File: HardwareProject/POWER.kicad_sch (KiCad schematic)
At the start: 42 parts, among them U11 TPS54302, U12 LP5907MFX-3.3, U13 REF3030, U14 LM5164DDA, U15 SY8089

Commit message: 修改了UCC27211A封装，此芯片此前的封装均错误 修改了采样线布局，为SAR ADC加入前置RC
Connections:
- net +5V: now also U12.3 (EN)
- net at C62.1, FB5.2, U12.1 (IN): no longer U12.3 (EN)
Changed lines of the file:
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@@
-	)
-	(junction
-		(at 74.93 27.94)
-		(diameter 0)
-		(color 0 0 0 0)
 	)
 	(junction
@@
 		(pts
 			(xy 100.33 130.81) (xy 105.41 130.81)
-		)
-		(stroke
-			(width 0)
-			(type default)
-		)
-	)
-	(wire
-		(pts
-			(xy 74.93 27.94) (xy 74.93 30.48)
 		)
 		(stroke
@@
 					(unit 1)
 				)
+			)
+		)
+	)
+	(symbol
+		(lib_id "power:+5V")
+		(at 74.93 30.48 180)
+		(unit 1)
+		(exclude_from_sim no)
+		(in_bom yes)
+		(on_board yes)
+		(dnp no)
+		(fields_autoplaced yes)
+		(property "Reference" "#PWR0190"
+			(at 74.93 26.67 0)
+			(effects
+				(font
+					(size 1.27 1.27)
+				)
+				(hide yes)
+			)
+		)
+		(property "Value" "+5V"
+			(at 74.93 35.56 0)
+			(effects
+				(font
+					(size 1.27 1.27)
+				)
+			)
+		)
+		(property "Footprint" ""
+			(at 74.93 30.48 0)
+			(effects
+				(font
+					(size 1.27 1.27)
+				)
+				(hide yes)
+			)
+		)
+		(property "Datasheet" ""
+			(at 74.93 30.48 0)
+			(effects
+				(font
+					(size 1.27 1.27)
+				)
+				(hide yes)
+			)
+		)
+		(property "Description" "Power symbol creates a global label with name \"+5V\""
+			(at 74.93 30.48 0)
+			(effects
+				(font
+					(size 1.27 1.27)
+				)
+				(hide yes)
+			)
+		)
+		(pin "1"
+		)
+		(instances
+			(project "HPM6P41_BB"
+				(path "/714b8a30-f9a7-49d4-a000-bc20c4884c7a/ae00fc9a-f385-4ed0-b801-78ac3a8c32a6"
+					(reference "#PWR0190")
+					(unit 1)
+				)

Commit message: 换掉UCC27519，它居然要55%VDD才到逻辑高，换成UCC2751
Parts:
- R48: value 309k -> 357k
- R54: value 101k -> 50k
- R63: value 665k -> 453k
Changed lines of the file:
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@@
 			)
 		)
-		(property "Value" "309k"
+		(property "Value" "357k"
 			(at 228.6 49.53 90)
 			(effects
@@
 			)
 		)
-		(property "Value" "101k"
+		(property "Value" "50k"
 			(at 248.92 66.04 90)
 			(effects
@@
 			)
 		)
-		(property "Value" "665k"
+		(property "Value" "453k"
 			(at 248.92 54.61 90)
 			(effects

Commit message: 外置核心电压SYR838以改善ADC噪声
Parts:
- removed FB6: 100Ω@100MHz 2A, Inductor_SMD:L_0603_1608Metric, symbol Device:FerriteBead
- added C34, C37, C38: 22uF,10V, Capacitor_SMD:C_0603_1608Metric, symbol Device:C
- added D20: DSS34, Diode_SMD:D_SOD-123F, symbol PCM_Diode_AKL:1N4148WF
- added L8: 2.2uH, Inductor_SMD:L_Changjiang_FNR252012S, symbol Device:L
- added R80, R81: 1kΩ, Resistor_SMD:R_0603_1608Metric, symbol Device:R
- added R82, R83, R84: 0Ω, Resistor_SMD:R_0603_1608Metric, symbol Device:R
- added U25: SYR838, kicad_community_lib:SYR838PKC, symbol SYR838PKC:SYR838PKC
- C58: value 22uF,35V -> 22uF,25V
- C66, C68: value 22uF -> 22uF,25V
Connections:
- net GNDPWR is gone; now on net GND: C70.2, C71.2, C77.2, R47.1, R54.1, U14.1 (GND), U14.9 (EP)
- net +5V: now also D20.1 (K), R83.1, R84.1; no longer L5.2
- net GND: now also C34.2, C37.2, C38.2, R81.1, U25.B2 (GND), U25.B3 (GND), U25.B4 (AGND), U25.C1 (GND), U25.C2 (GND), U25.C3 (GND), U25.C4 (GND)
- net at C72.1, U15.1 (EN), U15.4 (IN): now also R83.2
- new net: C37.1, L8.1, R82.1, U25.A4 (VOUT)
- new net: L8.2, U25.D3 (SW), U25.D4 (SW), U25.E3 (SW), U25.E4 (SW)
- new net: C34.1, R80.1, R84.2, U25.D1 (VIN), U25.D2 (VIN), U25.E1 (VIN), U25.E2 (VIN)
- new net: R81.2, U25.A1 (VSEL)
- new net: R80.2, U25.A2 (EN)
- new net: D20.2 (A), L5.2
- new net SYR838_SCL: U25.A3 (SCL)
- new net SYR838_SDA: U25.B1 (SDA)
- new net VDD_SOC: C38.1, R82.2
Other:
- note added: "12V-5V"
- note added: "VDD_SOC"
- note added: "驱动供电(12V)"
- note removed: "9.1V-5V"
- note removed: "驱动供电(9.1V)"
- moved on the sheet: C58, C59, C63, C64, C66, C68, C72, C74, C76, C78, FB3, L5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

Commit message: 换其他电感之前暂存一下
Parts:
- C58: value 22uF,25V -> 10uF,25V
- C59: value 100nF,50V -> 10uF,25V
- C66, C68: value 22uF,25V -> 22uF,10V; footprint Capacitor_SMD:C_0805_2012Metric -> Capacitor_SMD:C_0603_1608Metric
- C71: value 1uF 100V -> 10uF,25V; footprint Capacitor_SMD:C_1206_3216Metric -> Capacitor_SMD:C_0805_2012Metric
- L8: value 2.2uH -> 0.47uH
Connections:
- net +5V: now also L5.2; no longer D20.1 (K)
- net VIN: no longer C71.1
- net Vdrv: now also D20.2 (A); no longer FB3.1
- net at C58.1, C59.1, FB3.2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: now also C71.1
- new net: D20.1 (K), FB3.1
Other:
- moved on the sheet: D20

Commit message: 完成Rev4 电源 驱动 模拟 IO
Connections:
- net +5V: no longer U12.3 (EN)
- net at C62.1, FB5.2, U12.1 (IN): now also U12.3 (EN)
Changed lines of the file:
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@@
+	)
+	(junction
+		(at 74.93 27.94)
+		(diameter 0)
+		(color 0 0 0 0)
 	)
 	(junction
@@
 		(pts
 			(xy 152.4 115.57) (xy 161.29 115.57)
+		)
+		(stroke
+			(width 0)
+			(type default)
+		)
+	)
+	(wire
+		(pts
+			(xy 74.93 30.48) (xy 74.93 27.94)
 		)
 		(stroke
@@
 					(unit 1)
 				)
-			)
-		)
-	)
-	(symbol
-		(lib_id "power:+5V")
-		(at 74.93 30.48 180)
-		(unit 1)
-		(exclude_from_sim no)
-		(in_bom yes)
-		(on_board yes)
-		(dnp no)
-		(fields_autoplaced yes)
-		(property "Reference" "#PWR0190"
-			(at 74.93 26.67 0)
-			(effects
-				(font
-					(size 1.27 1.27)
-				)
-				(hide yes)
-			)
-		)
-		(property "Value" "+5V"
-			(at 74.93 35.56 0)
-			(effects
-				(font
-					(size 1.27 1.27)
-				)
-			)
-		)
-		(property "Footprint" ""
-			(at 74.93 30.48 0)
-			(effects
-				(font
-					(size 1.27 1.27)
-				)
-				(hide yes)
-			)
-		)
-		(property "Datasheet" ""
-			(at 74.93 30.48 0)
-			(effects
-				(font
-					(size 1.27 1.27)
-				)
-				(hide yes)
-			)
-		)
-		(property "Description" "Power symbol creates a global label with name \"+5V\""
-			(at 74.93 30.48 0)
-			(effects
-				(font
-					(size 1.27 1.27)
-				)
-				(hide yes)
-			)
-		)
-		(pin "1"
-		)
-		(instances
-			(project "HPM6P41_BB"
-				(path "/714b8a30-f9a7-49d4-a000-bc20c4884c7a/ae00fc9a-f385-4ed0-b801-78ac3a8c32a6"
-					(reference "#PWR0190")
-					(unit 1)
-				)

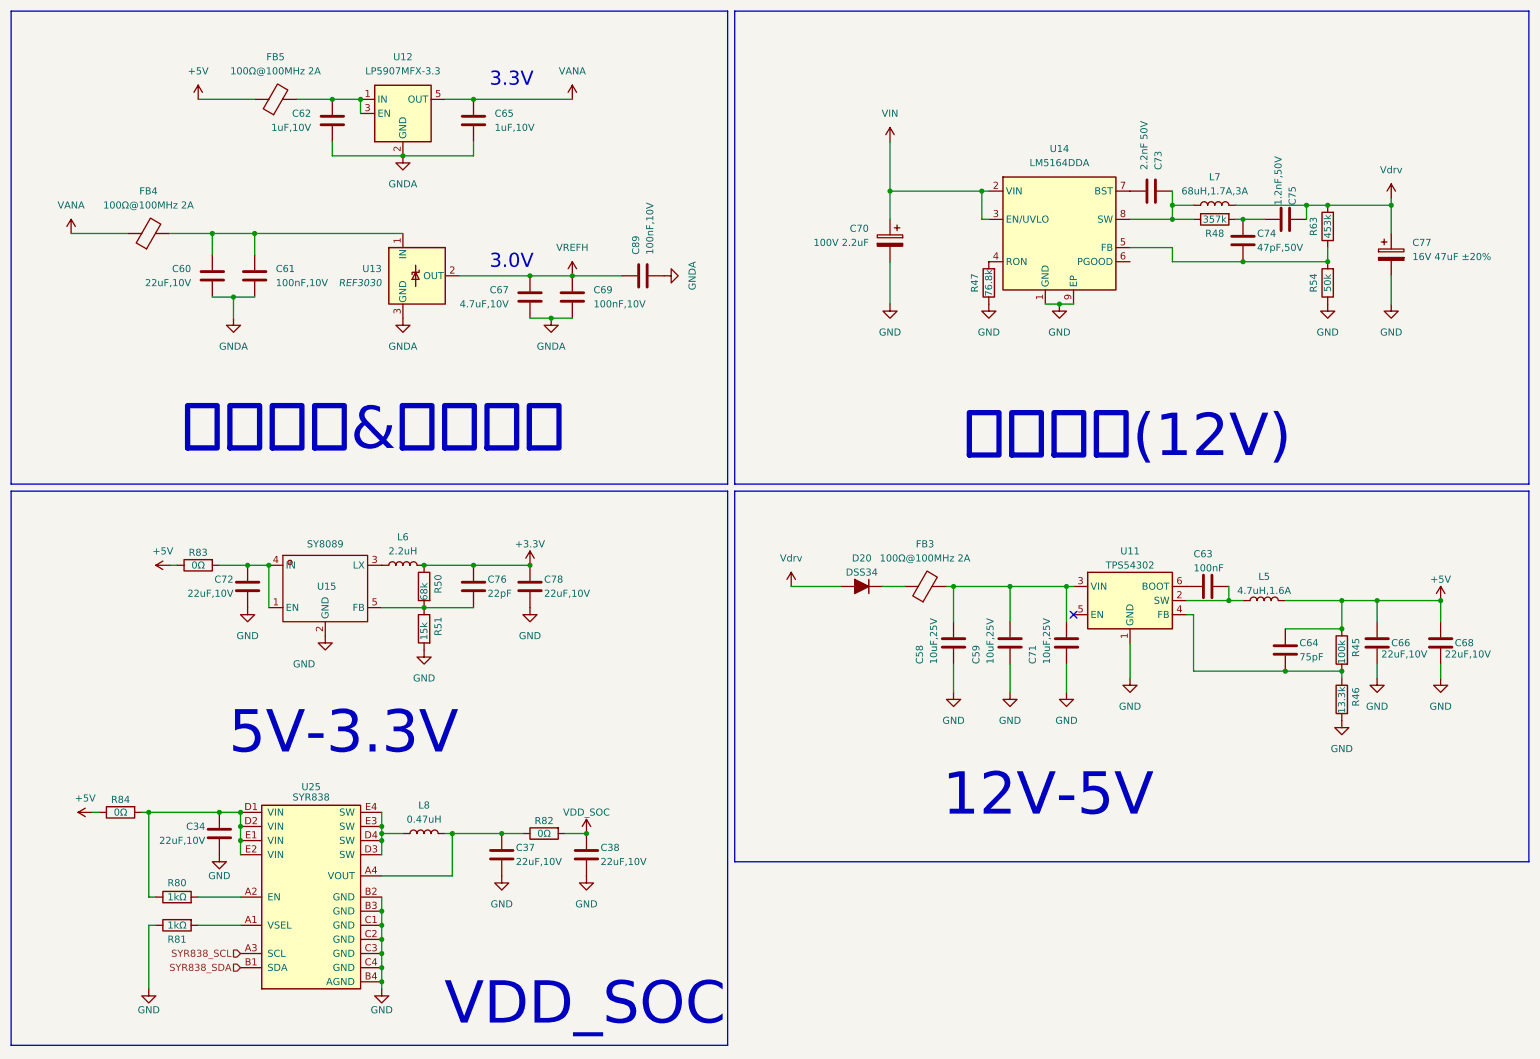
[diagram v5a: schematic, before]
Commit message: rev4修改核心供电前保存（当前SYR838）
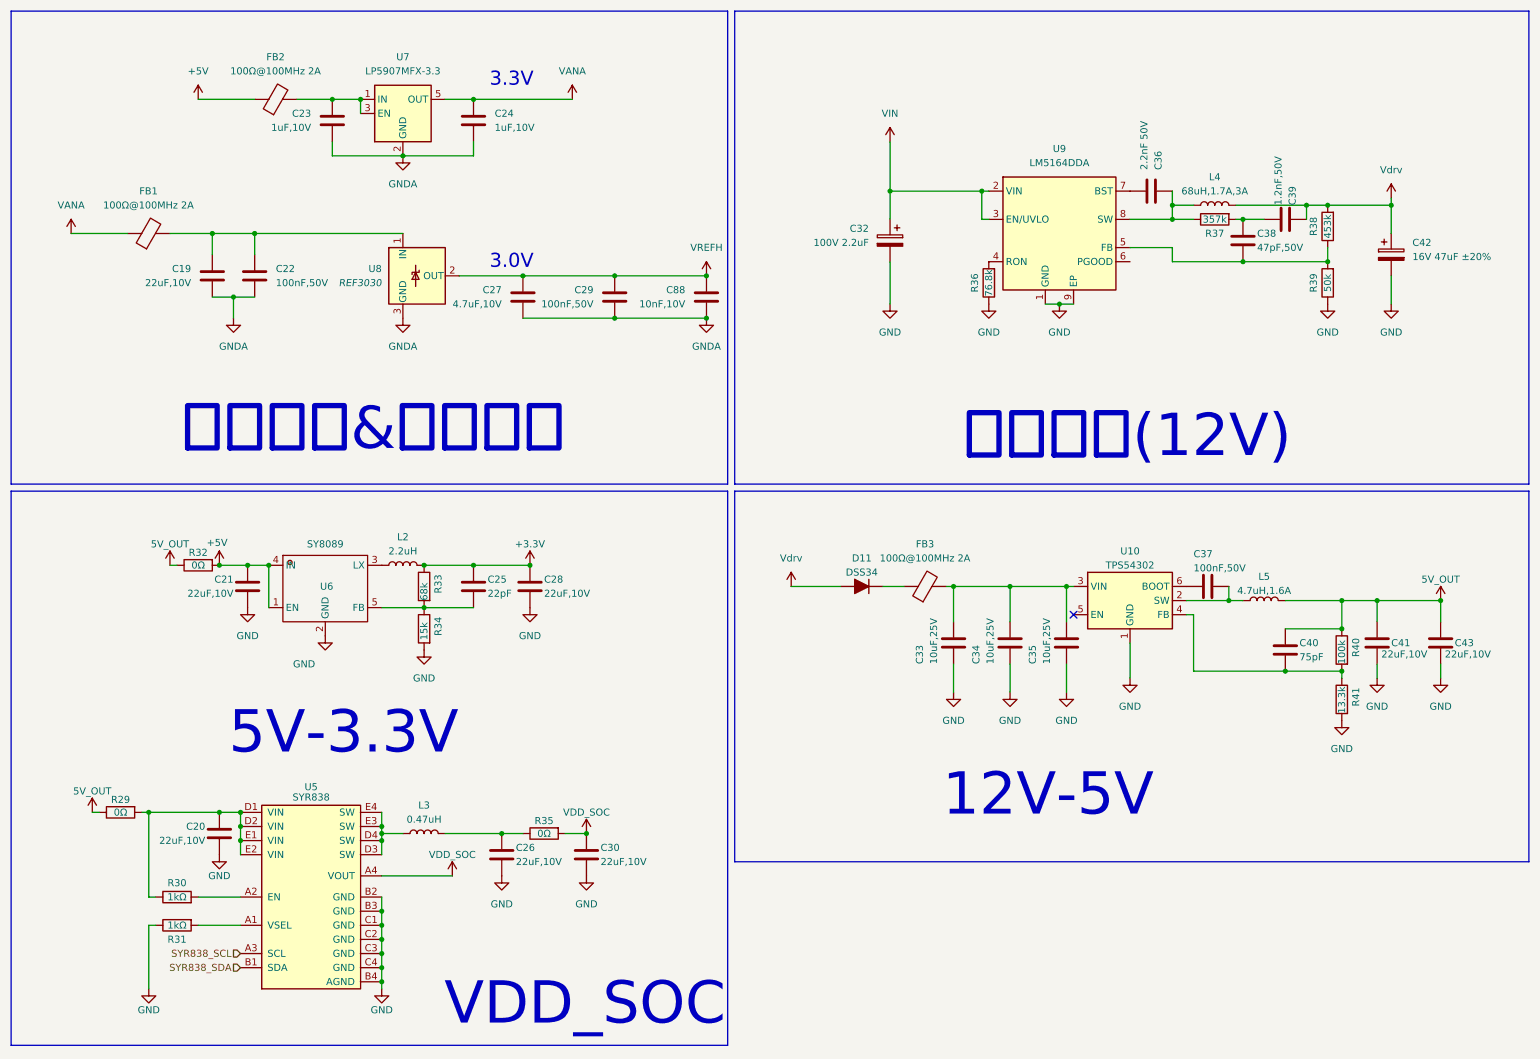
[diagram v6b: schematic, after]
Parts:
- removed C89: 100nF,10V, Capacitor_SMD:C_0603_1608Metric, symbol Device:C
- added C88: 10nF,10V, Capacitor_SMD:C_0603_1608Metric, symbol Device:C
- C22: renamed from C61; value 100nF,10V -> 100nF,50V
- C29: renamed from C69; value 100nF,10V -> 100nF,50V
- C37: renamed from C63; value 100nF -> 100nF,50V
- renumbered C60 to C19, C34 to C20, C72 to C21, C62 to C23, C65 to C24, C76 to C25, C37 to C26, C67 to C27, C78 to C28, C38 to C30, C70 to C32, C58 to C33, C59 to C34, C71 to C35, C73 to C36, C74 to C38, C75 to C39, C64 to C40, C66 to C41, C77 to C42, C68 to C43, D20 to D11, FB4 to FB1, FB5 to FB2, L6 to L2, L8 to L3, L7 to L4, R84 to R29, R80 to R30, R81 to R31, R83 to R32, R50 to R33, R51 to R34, R82 to R35, R47 to R36, R48 to R37, R63 to R38, R54 to R39, R45 to R40, R46 to R41, U11 to U10, U25 to U5, U15 to U6, U12 to U7, U13 to U8, U14 to U9
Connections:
- net +5V: now also C21.1, R32.2, U6.1 (EN), U6.4 (IN); no longer C40.1, C41.1, C43.1, L5.2, R29.1, R32.1, R40.1
- net GNDA: now also C88.2
- net VDD_SOC: now also U5.A4 (VOUT)
- net VREFH: now also C88.1
- net at C26.1, L3.1, R35.1: no longer U5.A4 (VOUT)
- new net 5V_OUT: C40.1, C41.1, C43.1, L5.2, R29.1, R32.1, R40.1
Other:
- moved on the sheet: C27, C29

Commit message: Rev4保存
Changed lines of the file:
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@@
 		(dnp no)
 		(property "Reference" "U6"
-			(at 68.834 115.57 0)
+			(at 68.58 105.918 0)
 			(effects
 				(font
